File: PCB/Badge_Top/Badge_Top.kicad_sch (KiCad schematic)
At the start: 29 parts, among them J1 Conn_01x04_Pin

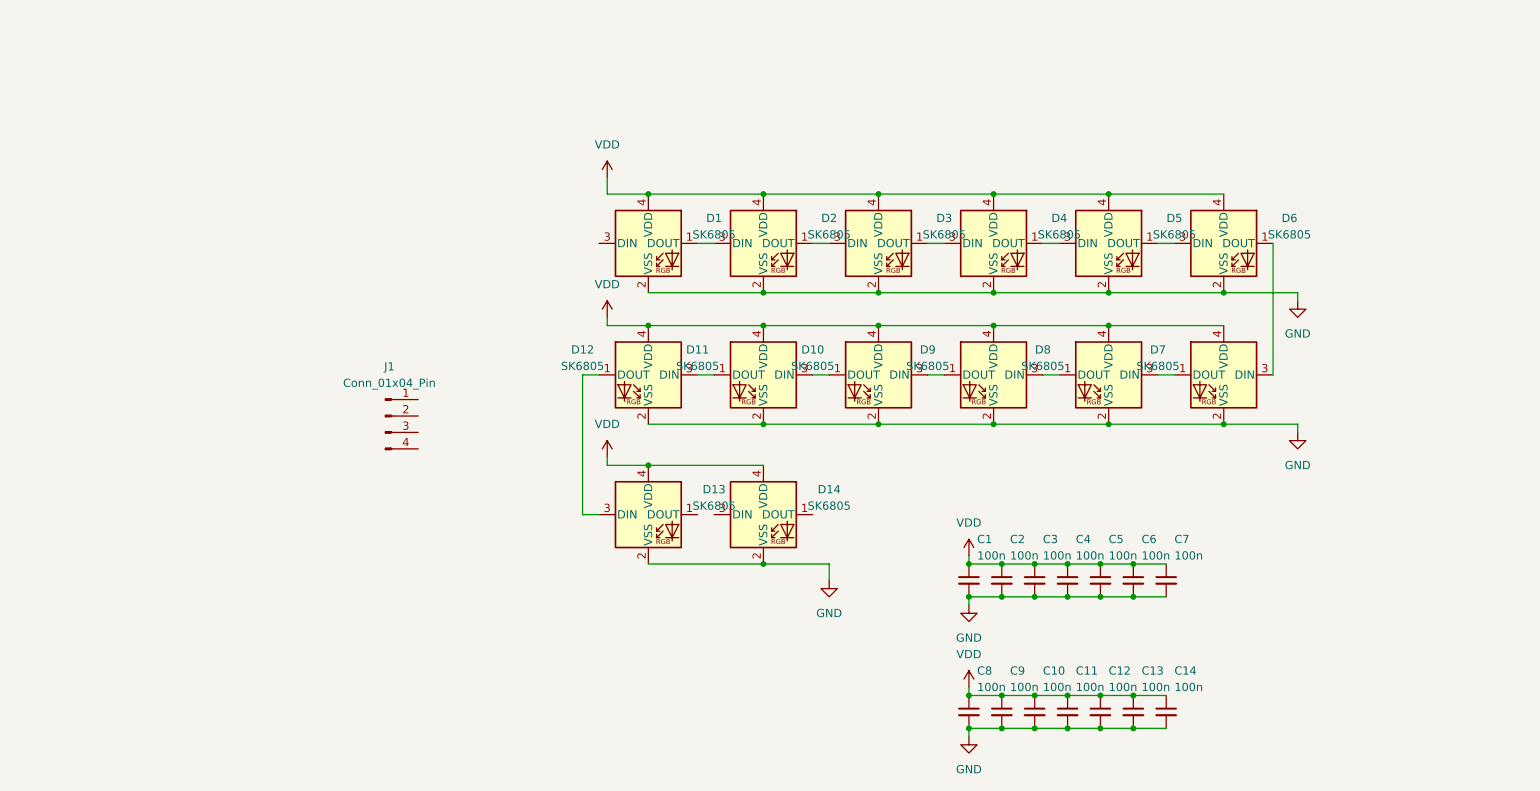
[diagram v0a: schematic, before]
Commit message: do layout of top PCB, generated preliminary gerbers
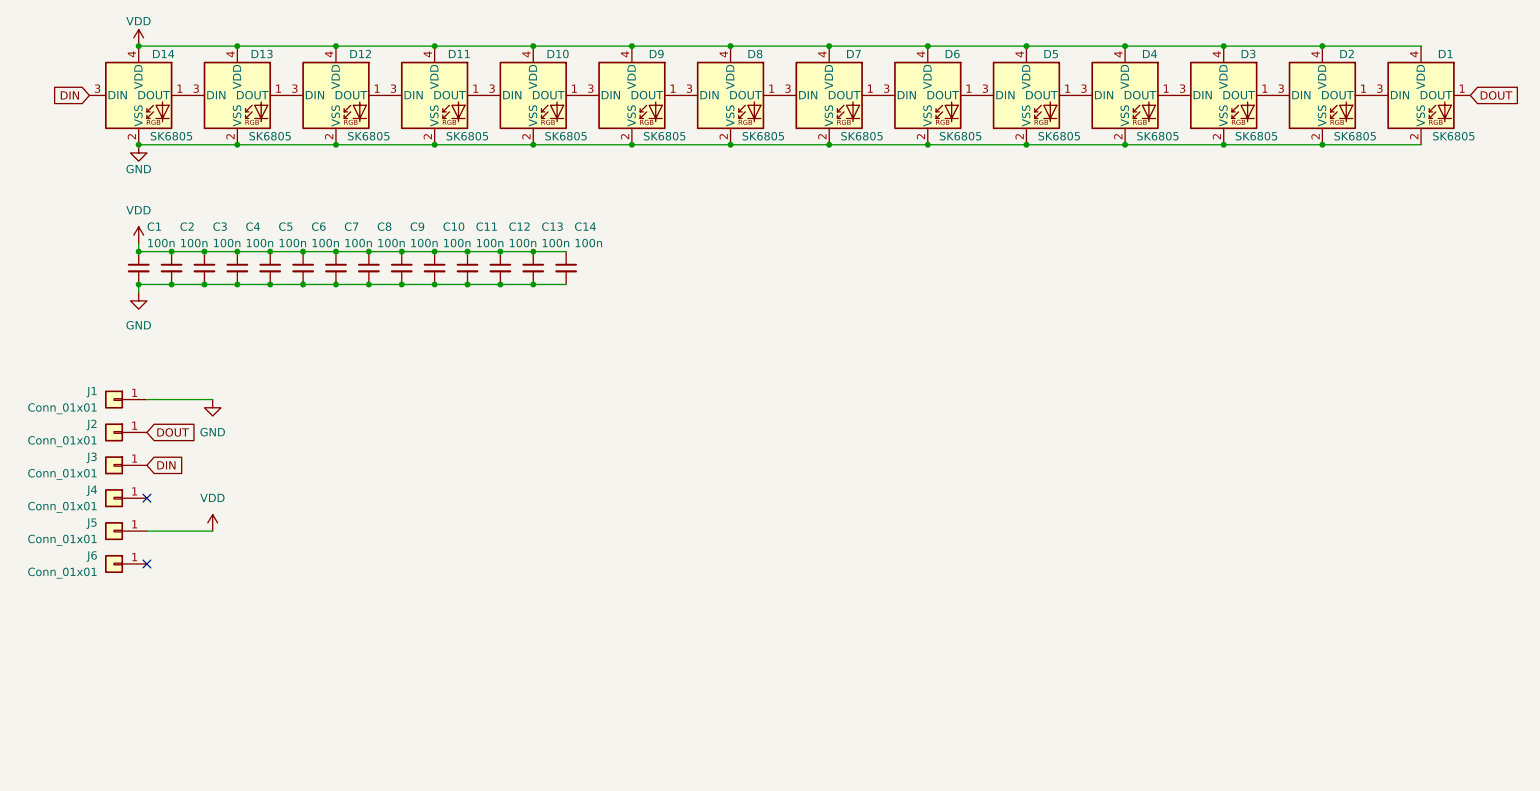
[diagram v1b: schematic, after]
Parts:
- removed J1: Conn_01x04_Pin, symbol Connector:Conn_01x04_Pin
- added J1, J2, J3, J4, J5, J6: Conn_01x01, Mounting_Wuerth:Mounting_Wuerth_WA-SMSI-M2_H7mm_9774070243, symbol Connector_Generic:Conn_01x01
- C1, C10, C11, C12, C13, C14, C2, C3, C4, C5, C6, C7, C8, C9: LCSC (none) -> C1525
- D1, D10, D11, D12, D13, D14, D2, D3, D4, D5, D6, D7, D8, D9: LCSC (none) -> C2909060
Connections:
- net GND: now also J1.1 (Pin_1)
- net VDD: now also J5.1 (Pin_1)
- net at D10.1 (DOUT): now also D9.3 (DIN); no longer D11.3 (DIN)
- net at D10.3 (DIN): now also D11.1 (DOUT); no longer D9.1 (DOUT)
- net at D6.1 (DOUT): now also D5.3 (DIN); no longer D7.3 (DIN)
- net at D6.3 (DIN): now also D7.1 (DOUT); no longer D5.1 (DOUT)
- net at D8.1 (DOUT): now also D7.3 (DIN); no longer D9.3 (DIN)
- net at D8.3 (DIN): now also D9.1 (DOUT); no longer D7.1 (DOUT)
- net at D2.3 (DIN): now also D3.1 (DOUT); no longer D1.1 (DOUT)
- net at D1.3 (DIN): now also D2.1 (DOUT)
- net at D12.1 (DOUT): now also D11.3 (DIN); no longer D13.3 (DIN)
- net at D12.3 (DIN): now also D13.1 (DOUT); no longer D11.1 (DOUT)
- net at D4.1 (DOUT): now also D3.3 (DIN); no longer D5.3 (DIN)
- net at D4.3 (DIN): now also D5.1 (DOUT); no longer D3.1 (DOUT)
- net at D14.1 (DOUT): now also D13.3 (DIN)
- net DIN: now reaches D14.3 (DIN)
- net DIN: now also J3.1 (Pin_1)
- new net DOUT: D1.1 (DOUT), J2.1 (Pin_1)
- no-connect marks 0 -> 2
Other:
- moved on the sheet: C1, C10, C11, C12, C13, C14, C2, C3, C4, C5, C6, C7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

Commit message: better silkscreen, remove DOUT
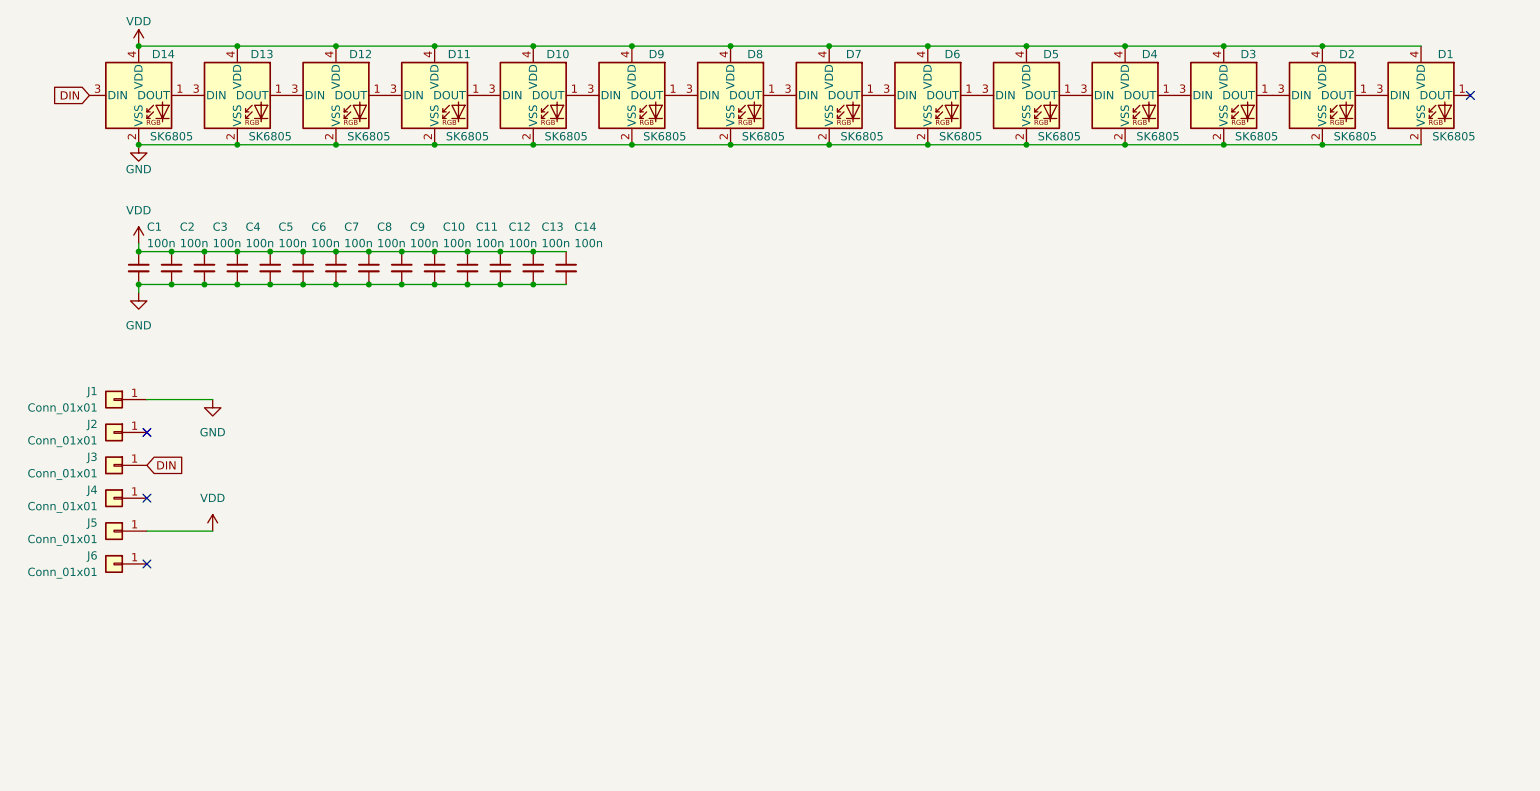
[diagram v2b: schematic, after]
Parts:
- J1, J2, J3, J4, J5, J6: LCSC C2928186 -> C2916355
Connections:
- net DOUT: no longer names the net of D1.1 (DOUT)
- net DOUT: no longer J2.1 (Pin_1)
- no-connect marks 2 -> 4
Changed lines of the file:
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@@
   )
   (no_connect (at 45.72 104.14))
+  (no_connect (at 45.72 93.98))
   (no_connect (at 45.72 114.3))
+  (no_connect (at 250.19 41.91))
   (wire (pts (xy 181.61 34.29) (xy 196.85 34.29))
     (stroke (width 0) (type default))
@@
   (wire (pts (xy 227.33 49.53) (xy 242.57 49.53))
     (stroke (width 0) (type default))
-  )
-  (global_label "DOUT" (shape input) (at 45.72 93.98 0) (fields_autoplaced)
-    (effects (font (size 1.27 1.27)) (justify left))
-    (property "Intersheetrefs" "${INTERSHEET_REFS}" (at 53.5244 93.98 0)
-      (effects (font (size 1.27 1.27)) (justify left) hide)
-    )
-  )
-  (global_label "DOUT" (shape input) (at 250.19 41.91 0) (fields_autoplaced)
-    (effects (font (size 1.27 1.27)) (justify left))
-    (property "Intersheetrefs" "${INTERSHEET_REFS}" (at 257.9944 41.91 0)
-      (effects (font (size 1.27 1.27)) (justify left) hide)
-    )
   )
   (global_label "DIN" (shape input) (at 45.72 99.06 0) (fields_autoplaced)
@@
       (effects (font (size 1.27 1.27)) hide)
     )
-    (property "LCSC" "C2928186" (at 38.1 107.95 0)
+    (property "LCSC" "C2916355" (at 38.1 107.95 0)
       (effects (font (size 1.27 1.27)) hide)
     )
@@
       (effects (font (size 1.27 1.27)) hide)
     )
-    (property "LCSC" "C2928186" (at 38.1 97.79 0)
+    (property "LCSC" "C2916355" (at 38.1 97.79 0)
       (effects (font (size 1.27 1.27)) hide)
     )
@@
       (effects (font (size 1.27 1.27)) hide)
     )
-    (property "LCSC" "C2928186" (at 38.1 113.03 0)
+    (property "LCSC" "C2916355" (at 38.1 113.03 0)
       (effects (font (size 1.27 1.27)) hide)
     )
@@
       (effects (font (size 1.27 1.27)) hide)
     )
-    (property "LCSC" "C2928186" (at 38.1 92.71 0)
+    (property "LCSC" "C2916355" (at 38.1 92.71 0)
       (effects (font (size 1.27 1.27)) hide)
     )
@@
       (effects (font (size 1.27 1.27)) hide)
     )
-    (property "LCSC" "C2928186" (at 38.1 87.63 0)
+    (property "LCSC" "C2916355" (at 38.1 87.63 0)
       (effects (font (size 1.27 1.27)) hide)
     )
@@
       (effects (font (size 1.27 1.27)) hide)
     )
-    (property "LCSC" "C2928186" (at 38.1 102.87 0)
-      (effects (font (size 1.27 1.27)) hide)
-    )
+    (property "LCSC" "C2916355" (at 38.1 102.87 0)
+      (effects (font (size 1.27 1.27)) hide)
+    )

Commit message: Added docs and readme, ordered PCBs at JLC
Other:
- company: (none) -> Unterland
- title: (none) -> Unterland Badge Top
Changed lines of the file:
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@@
 (kicad_sch (version 20230121) (generator eeschema)
   (paper "A4")
+  (title_block
+    (title "Unterland Badge Top")
+    (date "2023-07-29")
+    (rev "2")
+    (company "Unterland")
+  )
   (junction (at 166.37 34.29) (diameter 0) (color 0 0 0 0)
   )
